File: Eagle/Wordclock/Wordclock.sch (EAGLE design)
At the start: 281 parts, among them IC1 MEGA8-P, Q3 SUP75N06-08

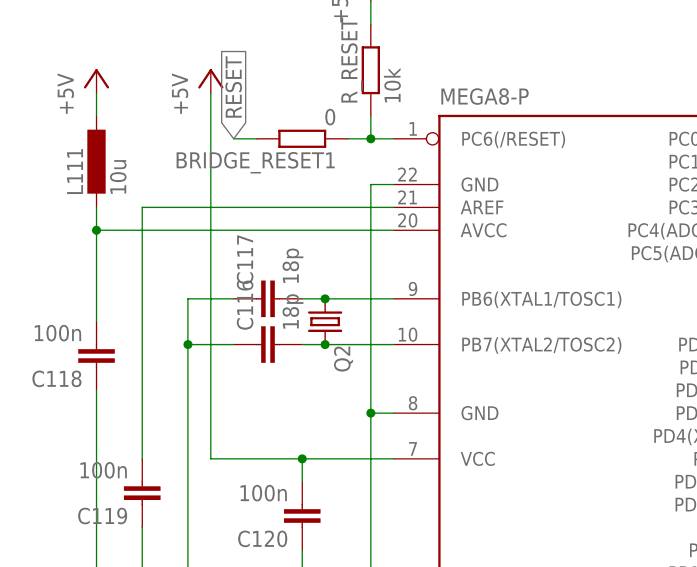
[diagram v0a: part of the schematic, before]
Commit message: Bestellung bei Reichelt und WS2812 und Kondensator auf 15p geändert
Bestellung bei Reichelt und WS2812 und Wert des Kondensator am AVR
Quarz auf 15p geändert
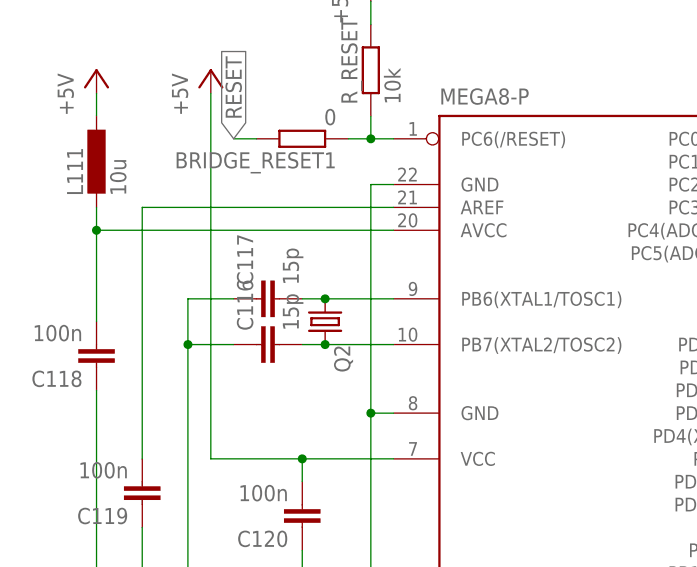
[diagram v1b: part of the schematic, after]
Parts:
- C116, C117: value 18p -> 15p
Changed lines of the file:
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@@
 <part name="C_S4" library="rcl" deviceset="C-EU" device="C1206" value="100n"/>
 <part name="R_S4" library="rcl" deviceset="R-EU_" device="M1206" value="1k"/>
-<part name="C116" library="rcl" deviceset="C-EU" device="C0805" value="18p"/>
-<part name="C117" library="rcl" deviceset="C-EU" device="C0805" value="18p"/>
+<part name="C116" library="rcl" deviceset="C-EU" device="C0805" value="15p"/>
+<part name="C117" library="rcl" deviceset="C-EU" device="C0805" value="15p"/>
 <part name="GND228" library="supply1" deviceset="GND" device=""/>
 <part name="SV1" library="con-harting-ml" deviceset="ML6" device="L"/>

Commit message: Versuch AVR Studio
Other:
- note added: "ACHTUNG !!!! DIE QUArze müssen neu gemacht werden und in ein anderes Gehäuse verbaut werde."
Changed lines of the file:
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@@
 <text x="-2.54" y="-208.28" size="1.778" layer="91">SCL/SDA fehlen in erstem
  entwickeltem Bord noch !!</text>
+<text x="-160.02" y="2.54" size="1.778" layer="91">ACHTUNG !!!!
+DIE QUArze müssen neu gemacht werden und in ein anderes Gehäuse verbaut werde.</text>
 </plain>
 <instances>
